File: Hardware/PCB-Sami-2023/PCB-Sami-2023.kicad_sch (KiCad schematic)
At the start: 16 parts, among them J1 Bateria (+), J10 MOTOR_DER, J2 IR_COSTADO, J3 Sensor TATAMI Derecho, J5 Sensor TATAMI Izquierdo, J6 STEP_DOWN, J7 IR_DER, J8 IR_IZQ, J9 MOTOR_IZQ, SW1 START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

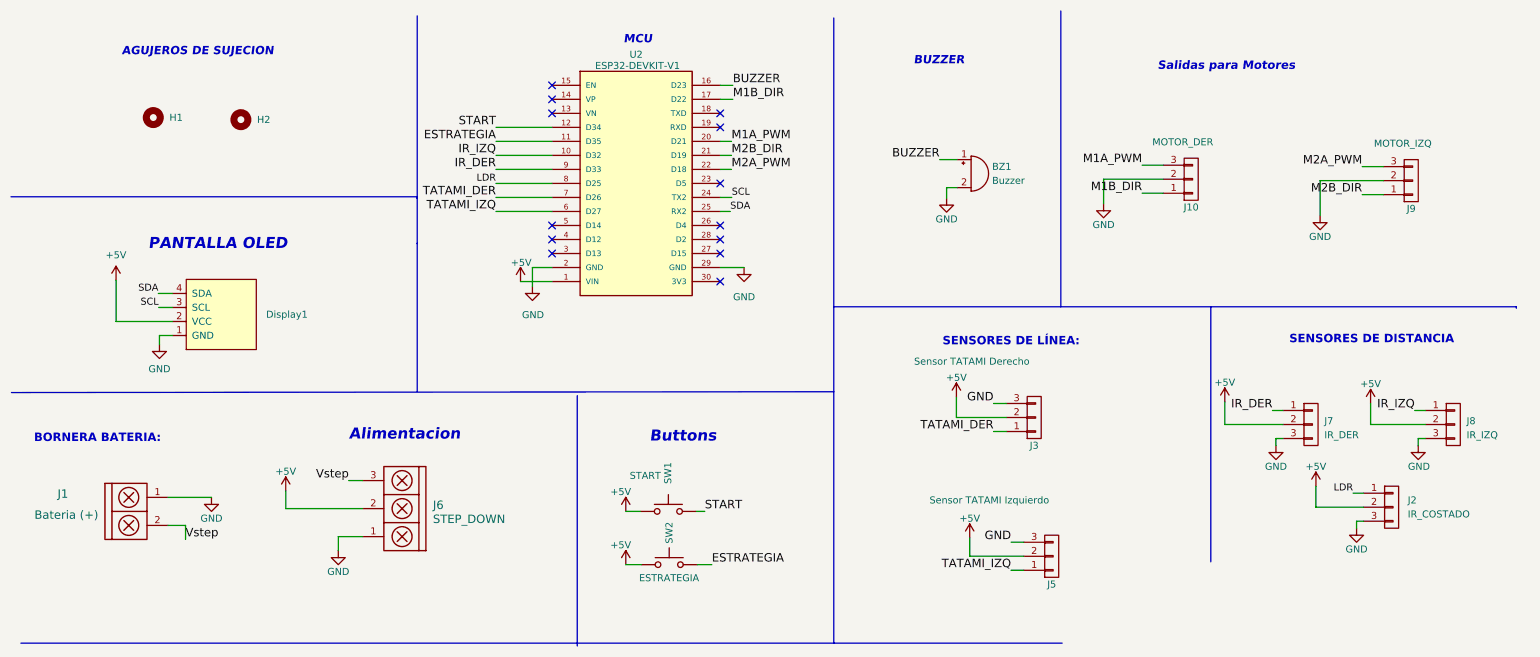
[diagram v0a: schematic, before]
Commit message: PCB con sus componentes correctamente acomodados, falta solo los agujeros de sujecion y trazar pistas
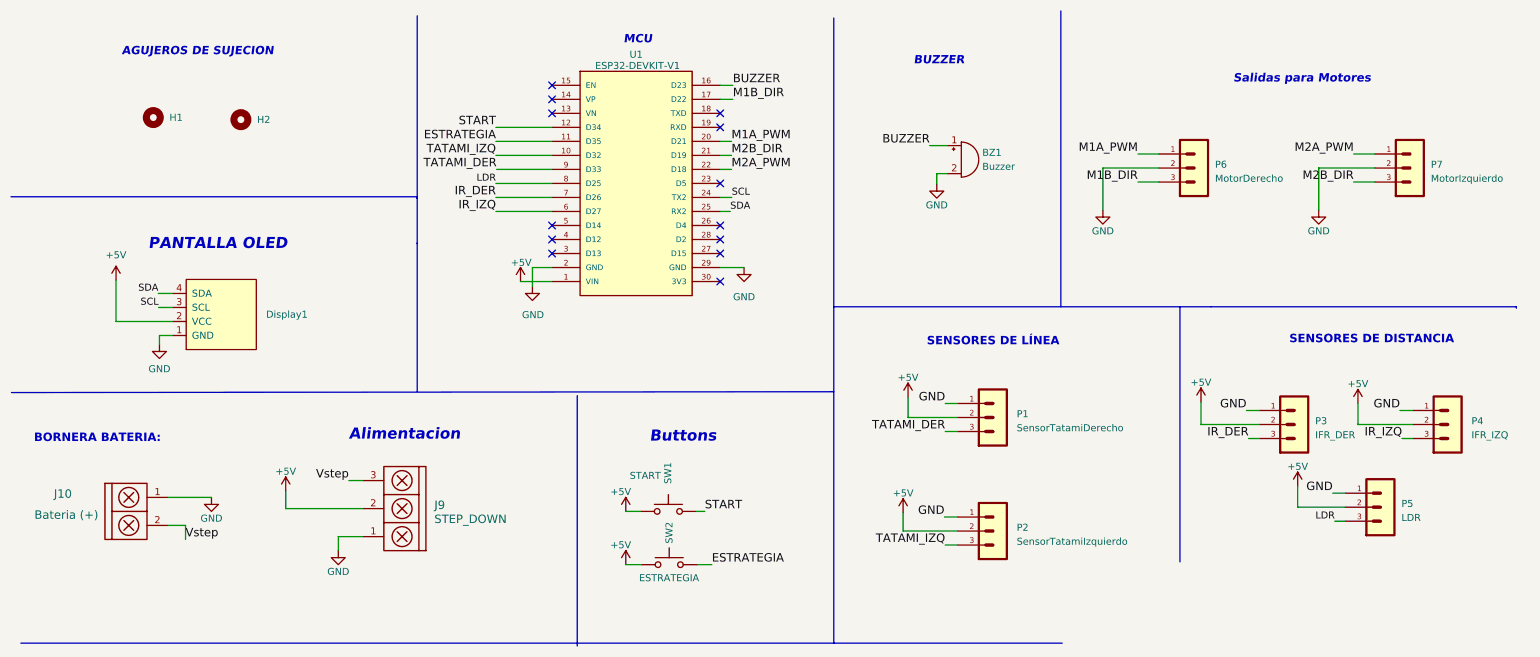
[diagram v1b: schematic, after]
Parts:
- removed J10: MOTOR_DER, EESTN5:Pin_Strip_3, symbol EESTN5:CONN_01X03
- removed J2: IR_COSTADO, EESTN5:Pin_Strip_3, symbol EESTN5:Conn_01X03
- removed J3: Sensor TATAMI Derecho, EESTN5:Pin_Strip_3, symbol EESTN5:CONN_01X03
- removed J5: Sensor TATAMI Izquierdo, EESTN5:Pin_Strip_3, symbol EESTN5:CONN_01X03
- removed J7: IR_DER, EESTN5:Pin_Strip_3, symbol EESTN5:Conn_01X03
- removed J8: IR_IZQ, EESTN5:Pin_Strip_3, symbol EESTN5:Conn_01X03
- removed J9: MOTOR_IZQ, EESTN5:Pin_Strip_3, symbol EESTN5:CONN_01X03
- added P1: SensorTatamiDerecho, Footprints:JstXH3P, symbol Librerias:JST-XH-3P
- added P2: SensorTatamiIzquierdo, Footprints:JstXH3P, symbol Librerias:JST-XH-3P
- added P3: IFR_DER, Footprints:JstXH3P, symbol Librerias:JST-XH-3P
- added P4: IFR_IZQ, Footprints:JstXH3P, symbol Librerias:JST-XH-3P
- added P5: LDR, EESTN5:Pin_Strip_3, symbol Librerias:JST-XH-3P
- added P6: MotorDerecho, Footprints:JstXH3P, symbol Librerias:JST-XH-3P
- added P7: MotorIzquierdo, Footprints:JstXH3P, symbol Librerias:JST-XH-3P
- renumbered J1 to J10, J6 to J9, U2 to U1
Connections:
- net +5V: now also P1.2, P2.2, P3.2, P4.2, P5.2
- net GND: now also P1.1, P2.1, P3.1, P4.1, P5.1, P6.2, P7.2
- net IR_DER: now also U1.7 (D26), P3.3; no longer U1.9 (D33)
- net IR_IZQ: now also U1.6 (D27), P4.3; no longer U1.10 (D32)
- net LDR: now also P5.3
- net M1A_PWM: now also P6.1
- net M1B_DIR: now also P6.3
- net M2A_PWM: now also P7.1
- net M2B_DIR: now also P7.3
- net TATAMI_DER: now also U1.9 (D33), P1.3; no longer U1.7 (D26)
- net TATAMI_IZQ: now also U1.10 (D32), P2.3; no longer U1.6 (D27)
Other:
- note added: "SENSORES DE LÍNEA"
- note removed: "SENSORES DE LÍNEA:"
- moved on the sheet: BZ1

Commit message: placa terminada
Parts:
- BZ1: footprint EESTN5:Pin_strip_2 -> EESTN5:Buzzer_12mm
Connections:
- net BUZZER: no longer U1.16 (D23)
- net IR_DER: now also U1.6 (D27); no longer U1.7 (D26)
- net IR_IZQ: now also U1.7 (D26); no longer U1.6 (D27)
- net LDR: now also U1.16 (D23); no longer U1.8 (D25)
- net TATAMI_DER: now also U1.8 (D25); no longer U1.9 (D33)
- net TATAMI_IZQ: now also U1.9 (D33); no longer U1.10 (D32)
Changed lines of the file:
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@@
     (stroke (width 0) (type default))
   )
-  (wire (pts (xy 100.076 38.354) (xy 110.236 38.354))
-    (stroke (width 0) (type default))
-  )
   (polyline (pts (xy 13.97 126.746) (xy 161.29 126.746))
     (stroke (width 0) (type default))
@@
     (effects (font (size 1.27 1.27)) (justify left bottom))
   )
+  (label "IR_DER" (at 100.076 48.514 180) (fields_autoplaced)
+    (effects (font (size 1.524 1.524)) (justify right bottom))
+  )
   (label "M1A_PWM" (at 142.748 35.814 0) (fields_autoplaced)
     (effects (font (size 1.524 1.524)) (justify left bottom))
@@
     (effects (font (size 1.524 1.524)) (justify right bottom))
   )
-  (label "IR_DER" (at 100.076 45.974 180) (fields_autoplaced)
-    (effects (font (size 1.524 1.524)) (justify right bottom))
-  )
   (label "IR_DER" (at 236.474 89.662 180) (fields_autoplaced)
     (effects (font (size 1.524 1.524)) (justify right bottom))
@@
     (effects (font (size 1.524 1.524)) (justify right bottom))
   )
+  (label "IR_IZQ" (at 100.076 45.974 180) (fields_autoplaced)
+    (effects (font (size 1.524 1.524)) (justify right bottom))
+  )
+  (label "TATAMI_DER" (at 100.076 43.434 180) (fields_autoplaced)
+    (effects (font (size 1.524 1.524)) (justify right bottom))
+  )
   (label "M2A_PWM" (at 255.524 38.1 180) (fields_autoplaced)
     (effects (font (size 1.524 1.524)) (justify right bottom))
@@
     (effects (font (size 1.524 1.524)) (justify right bottom))
   )
-  (label "TATAMI_IZQ" (at 100.076 38.354 180) (fields_autoplaced)
-    (effects (font (size 1.524 1.524)) (justify right bottom))
-  )
   (label "SCL" (at 38.9382 65.913 180) (fields_autoplaced)
     (effects (font (size 1.27 1.27)) (justify right bottom))
@@
     (effects (font (size 1.524 1.524)) (justify right bottom))
   )
-  (label "LDR" (at 100.076 43.434 180) (fields_autoplaced)
-    (effects (font (size 1.27 1.27)) (justify right bottom))
-  )
   (label "M1A_PWM" (at 216.408 38.1 180) (fields_autoplaced)
     (effects (font (size 1.524 1.524)) (justify right bottom))
@@
     (effects (font (size 1.524 1.524)) (justify right bottom))
   )
-  (label "TATAMI_DER" (at 100.203 40.894 180) (fields_autoplaced)
-    (effects (font (size 1.524 1.524)) (justify right bottom))
-  )
   (label "LDR" (at 252.095 104.648 180) (fields_autoplaced)
     (effects (font (size 1.27 1.27)) (justify right bottom))
@@
     (effects (font (size 1.524 1.524)) (justify right bottom))
   )
-  (label "BUZZER" (at 143.002 25.654 0) (fields_autoplaced)
-    (effects (font (size 1.524 1.524)) (justify left bottom))
+  (label "LDR" (at 143.002 25.654 0) (fields_autoplaced)
+    (effects (font (size 1.27 1.27)) (justify left bottom))
   )
-  (label "GND" (at 236.093 84.582 180) (fields_autoplaced)
+  (label "TATAMI_IZQ" (at 100.203 40.894 180) (fields_autoplaced)
     (effects (font (size 1.524 1.524)) (justify right bottom))
   )
-  (label "BUZZER" (at 178.689 36.576 180) (fields_autoplaced)
+  (label "GND" (at 236.093 84.582 180) (fields_autoplaced)
     (effects (font (size 1.524 1.524)) (justify right bottom))
   )
-  (label "IR_IZQ" (at 100.076 48.514 180) (fields_autoplaced)
+  (label "BUZZER" (at 178.689 36.576 180) (fields_autoplaced)
     (effects (font (size 1.524 1.524)) (justify right bottom))
   )
@@
       (effects (font (size 1.27 1.27)) (justify left))
     )
-    (property "Footprint" "EESTN5:Pin_strip_2" (at 183.769 36.576 90)
+    (property "Footprint" "EESTN5:Buzzer_12mm" (at 183.769 36.576 90)
       (effects (font (size 1.27 1.27)) hide)
     )

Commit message: PCB terminado
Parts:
- removed BZ1: Buzzer, EESTN5:Buzzer_12mm, symbol EESTN5:Buzzer
- removed Display1: SSD1306-SSD1306-128x64_OLED, EESTN5:128x64OLED, symbol EESTN5:SSD1306-SSD1306-128x64_OLED
- added P8: Pantalla Oled, Footprints:JstXH4P, symbol Librerias:JST-XH-4P
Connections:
- net +5V: now also P8.3
- net GND: now also P6.1, P7.1, P8.4; no longer P6.2, P7.2
- net M1A_PWM: now also P6.3, U1.17 (D22); no longer P6.1, U1.20 (D21)
- net M1B_DIR: now also P6.2, U1.20 (D21); no longer P6.3, U1.17 (D22)
- net M2A_PWM: now also P7.3, U1.21 (D19); no longer P7.1, U1.22 (D18)
- net M2B_DIR: now also P7.2, U1.22 (D18); no longer P7.3, U1.21 (D19)
- net SCL: now also P8.2
- net SDA: now also P8.1
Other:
- note removed: "BUZZER"

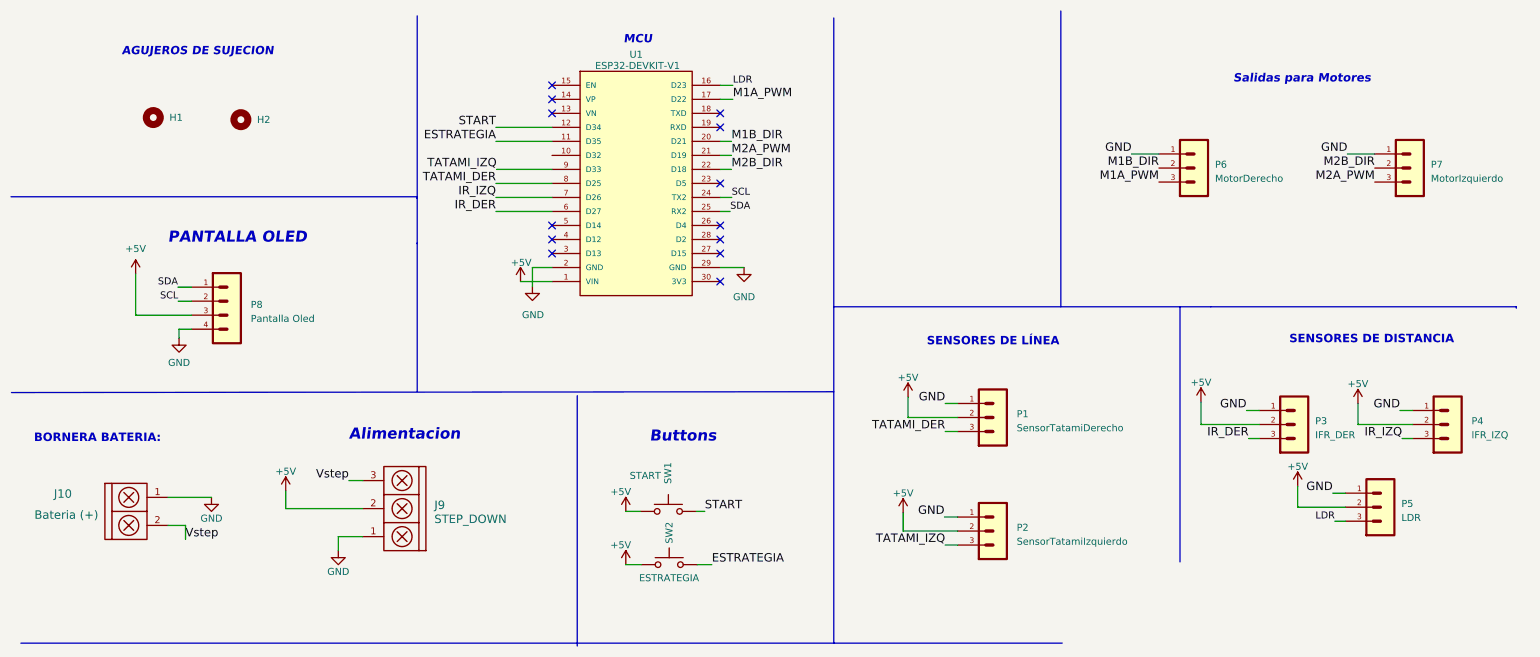
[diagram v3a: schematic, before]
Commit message: Corregi algunos errores de la placa
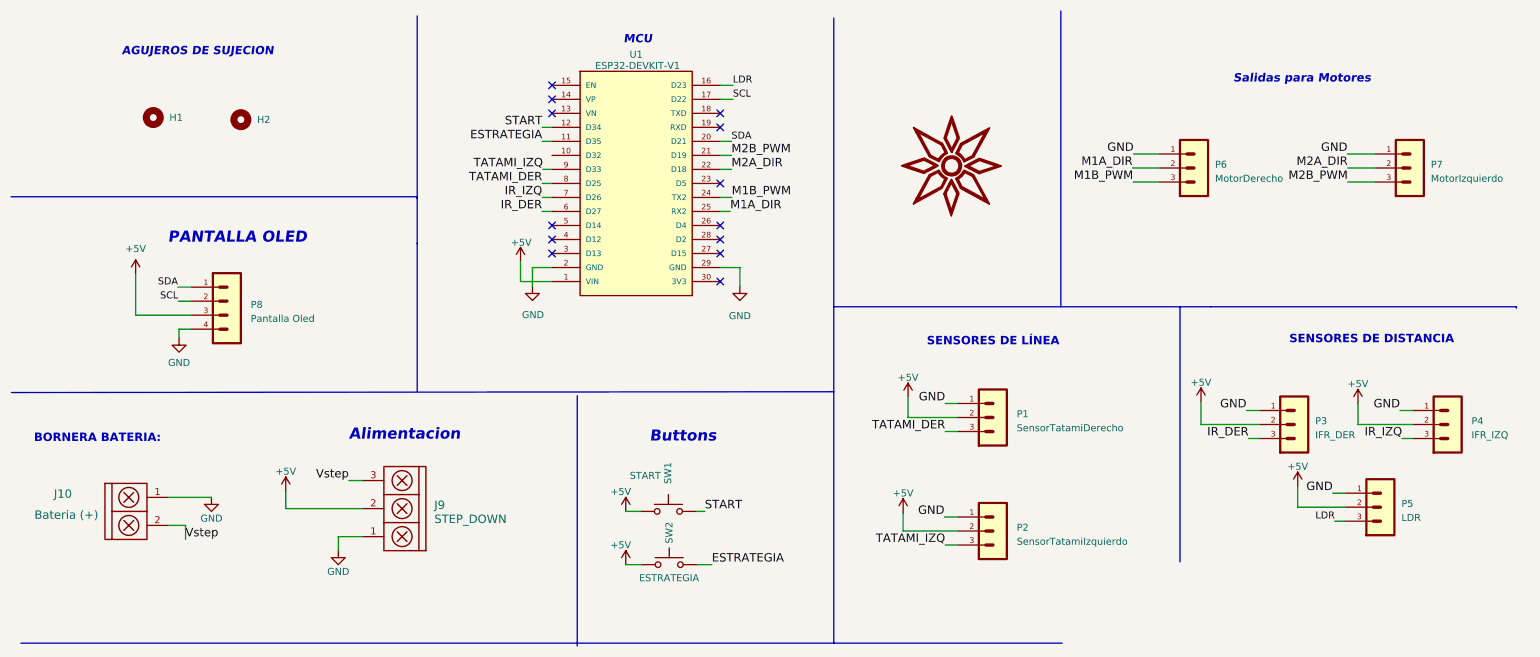
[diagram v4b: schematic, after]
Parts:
- added G1: LOGO, footprints:LogoSami2, symbol Librerias:LogoSami_2
- P1, P2, P3, P4, P6, P7: footprint Footprints:JstXH3P -> footprints:JstXH3P
- P8: footprint Footprints:JstXH4P -> footprints:JstXH4P
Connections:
- net SCL: now also U1.17 (D22); no longer U1.24 (TX2)
- net SDA: now also U1.20 (D21); no longer U1.25 (RX2)
- net M1A_PWM renamed M1B_PWM
- net M1B_PWM: now also U1.24 (TX2); no longer U1.17 (D22)
- net M1B_DIR renamed M1A_DIR
- net M1A_DIR: now also U1.25 (RX2); no longer U1.20 (D21)
- net M2A_PWM renamed M2B_PWM
- net M2B_DIR renamed M2A_DIR

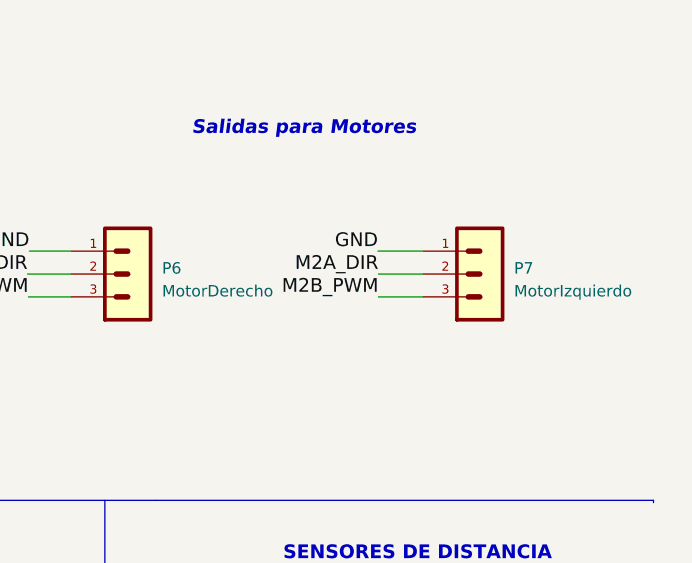
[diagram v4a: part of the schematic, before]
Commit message: agregue el archivo svg para la seligrafia
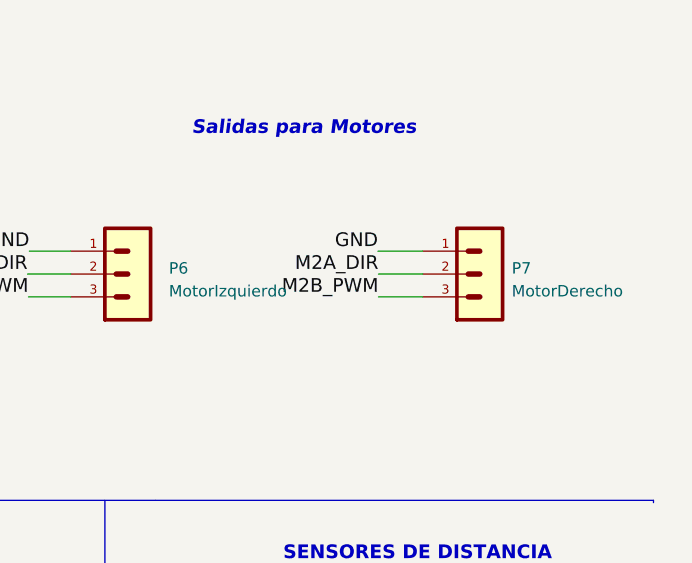
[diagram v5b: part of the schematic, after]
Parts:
- P6: value MotorDerecho -> MotorIzquierdo
- P7: value MotorIzquierdo -> MotorDerecho
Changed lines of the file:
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@@
   (symbol (lib_id "Librerias:JST-XH-3P") (at 264.414 40.64 0) (unit 1)
     (in_bom yes) (on_board yes) (dnp no) (fields_autoplaced)
-    (property "Reference" "P7" (at 269.494 40.005 0)
+    (property "Reference" "P7" (at 269.24 40.005 0)
       (effects (font (size 1.27 1.27)) (justify left))
     )
-    (property "Value" "MotorIzquierdo" (at 269.494 42.545 0)
+    (property "Value" "MotorDerecho" (at 269.24 42.545 0)
       (effects (font (size 1.27 1.27)) (justify left))
     )
@@
   (symbol (lib_id "Librerias:JST-XH-3P") (at 225.298 40.64 0) (unit 1)
     (in_bom yes) (on_board yes) (dnp no) (fields_autoplaced)
-    (property "Reference" "P6" (at 230.378 40.005 0)
+    (property "Reference" "P6" (at 231.14 40.005 0)
       (effects (font (size 1.27 1.27)) (justify left))
     )
-    (property "Value" "MotorDerecho" (at 230.378 42.545 0)
+    (property "Value" "MotorIzquierdo" (at 231.14 42.545 0)
       (effects (font (size 1.27 1.27)) (justify left))
     )
